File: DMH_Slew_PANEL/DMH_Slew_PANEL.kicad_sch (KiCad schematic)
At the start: 5 parts, among them J0 Panel_GND_Solder_Wire_Pad

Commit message: Started panel design
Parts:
- added H10: Out B, SynthStuff:Jack_6.35mm_Cutout_Output_v6, symbol SynthStuff:MountingHole_Jack6.35mm_Output_v2
- added H11: Mult In B, SynthStuff:Jack_6.35mm_Cutout_v3, symbol SynthStuff:MountingHole_Jack6.35mm_v2
- added H12: Mult In A, SynthStuff:Jack_6.35mm_Cutout_v3, symbol SynthStuff:MountingHole_Jack6.35mm_v2
- added H13: Mult Out A 1, SynthStuff:Jack_6.35mm_Cutout_Output_v6, symbol SynthStuff:MountingHole_Jack6.35mm_Output_v2
- added H14: Mult Out A 2, SynthStuff:Jack_6.35mm_Cutout_Output_v6, symbol SynthStuff:MountingHole_Jack6.35mm_Output_v2
- added H15: Mult Out B 1, SynthStuff:Jack_6.35mm_Cutout_Output_v6, symbol SynthStuff:MountingHole_Jack6.35mm_Output_v2
- added H16: Mult Out B 2, SynthStuff:Jack_6.35mm_Cutout_Output_v6, symbol SynthStuff:MountingHole_Jack6.35mm_Output_v2
- added H17, H19: Slew A, SynthStuff:Pot_Cutout_Small, symbol SynthStuff:MountingHole_Pot
- added H18, H20: CV Amt A, SynthStuff:Pot_Cutout_Tiny_attv_P110KH1, symbol SynthStuff:MountingHole_Pot
- added H5: In A, SynthStuff:Jack_6.35mm_Cutout_v3, symbol SynthStuff:MountingHole_Jack6.35mm_v2
- added H6: CV A, SynthStuff:Jack_6.35mm_Cutout_v3, symbol SynthStuff:MountingHole_Jack6.35mm_v2
- added H7: Out A, SynthStuff:Jack_6.35mm_Cutout_Output_v6, symbol SynthStuff:MountingHole_Jack6.35mm_Output_v2
- added H8: In B, SynthStuff:Jack_6.35mm_Cutout_v3, symbol SynthStuff:MountingHole_Jack6.35mm_v2
- added H9: CV B, SynthStuff:Jack_6.35mm_Cutout_v3, symbol SynthStuff:MountingHole_Jack6.35mm_v2
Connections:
- net GND: now also H10.1, H11.1, H12.1, H13.1, H14.1, H15.1, H16.1, H17.1, H18.1, H19.1, H20.1, H5.1, H6.1, H7.1, H8.1, H9.1

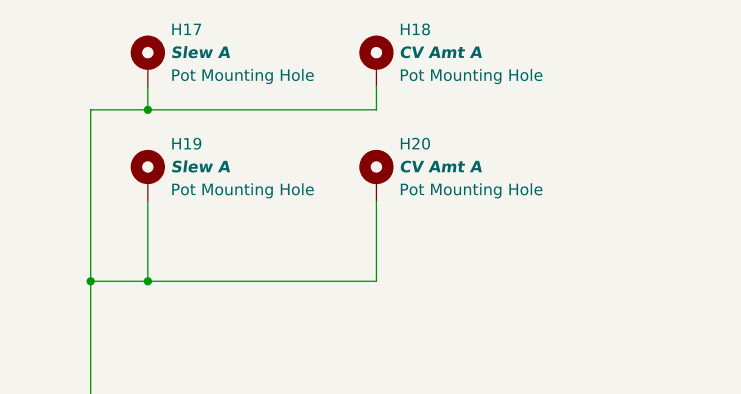
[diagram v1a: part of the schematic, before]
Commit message: Designed front panel
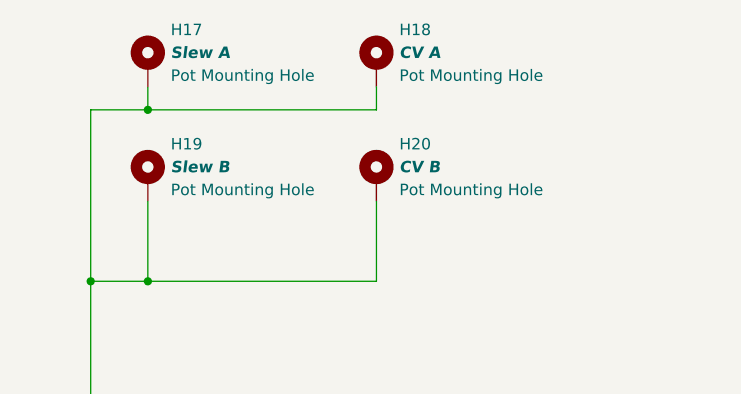
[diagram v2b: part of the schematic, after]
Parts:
- H18: value CV Amt A -> CV A
- H19: value Slew A -> Slew B
- H20: value CV Amt A -> CV B
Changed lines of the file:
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@@
 			)
 		)
-		(property "Value" "Slew A"
+		(property "Value" "Slew B"
 			(at 40.64 127 0)
 			(effects
@@
 			)
 		)
-		(property "Value" "CV Amt A"
+		(property "Value" "CV A"
 			(at 66.04 114.3 0)
 			(effects
@@
 			)
 		)
-		(property "Value" "CV Amt A"
+		(property "Value" "CV B"
 			(at 66.04 127 0)
 			(effects

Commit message: Redesign ongoing
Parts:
- added H21, H22: Shape, SynthStuff:Toggle_Switch_TE_Cutout, symbol SynthStuff:MountingHole_ToggleSwitch
- added H23: Mode, SynthStuff:Toggle_Switch_TE_Cutout, symbol SynthStuff:MountingHole_ToggleSwitch
- H11, J0: now not fitted
- H18, H6: value CV A -> CV A [R]
- H20, H9: value CV B -> CV B [F]
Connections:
- net GND: now also H21.1, H22.1, H23.1

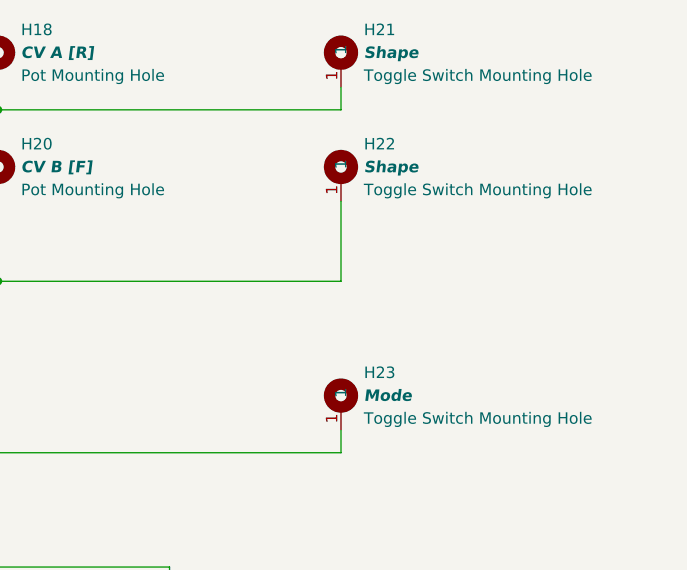
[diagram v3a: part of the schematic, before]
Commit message: Redesigned front panel
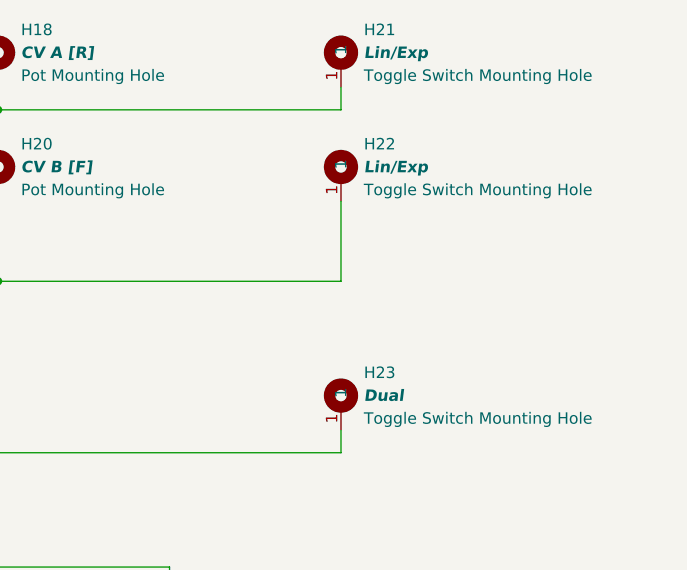
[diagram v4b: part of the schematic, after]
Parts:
- H21, H22: value Shape -> Lin/Exp
- H23: value Mode -> Dual
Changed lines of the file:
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@@
 			)
 		)
-		(property "Value" "Shape"
+		(property "Value" "Lin/Exp"
 			(at 104.14 114.3 0)
 			(effects
@@
 			)
 		)
-		(property "Value" "Shape"
+		(property "Value" "Lin/Exp"
 			(at 104.14 127 0)
 			(effects
@@
 			)
 		)
-		(property "Value" "Mode"
+		(property "Value" "Dual"
 			(at 104.14 152.4 0)
 			(effects

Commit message: Schematic design in progress
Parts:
- H23: value Dual -> A & B
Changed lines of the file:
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@@
 			)
 		)
-		(property "Value" "Dual"
+		(property "Value" "A & B"
 			(at 104.14 152.4 0)
 			(effects

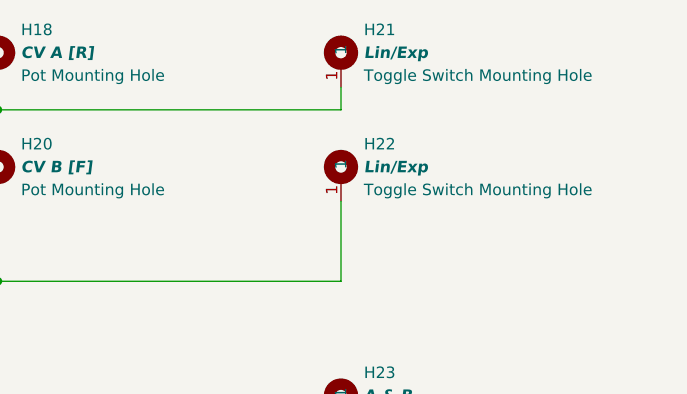
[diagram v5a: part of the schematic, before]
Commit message: Applied 10V to pots
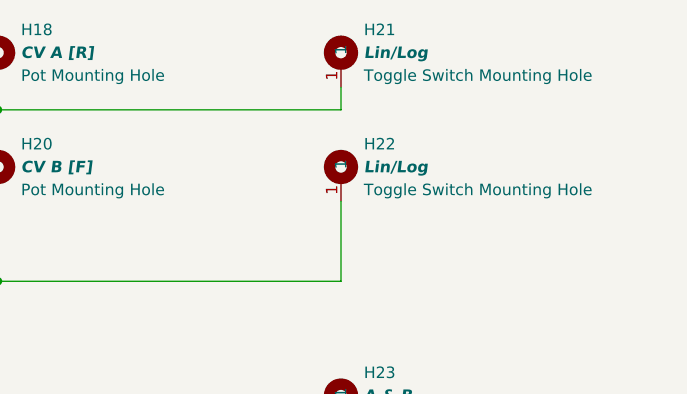
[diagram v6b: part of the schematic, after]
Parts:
- H21, H22: value Lin/Exp -> Lin/Log
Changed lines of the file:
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@@
 			)
 		)
-		(property "Value" "Lin/Exp"
+		(property "Value" "Lin/Log"
 			(at 104.14 114.3 0)
 			(effects
@@
 			)
 		)
-		(property "Value" "Lin/Exp"
+		(property "Value" "Lin/Log"
 			(at 104.14 127 0)
 			(effects
